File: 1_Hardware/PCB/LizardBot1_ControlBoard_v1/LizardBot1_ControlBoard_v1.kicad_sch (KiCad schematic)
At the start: 12 parts

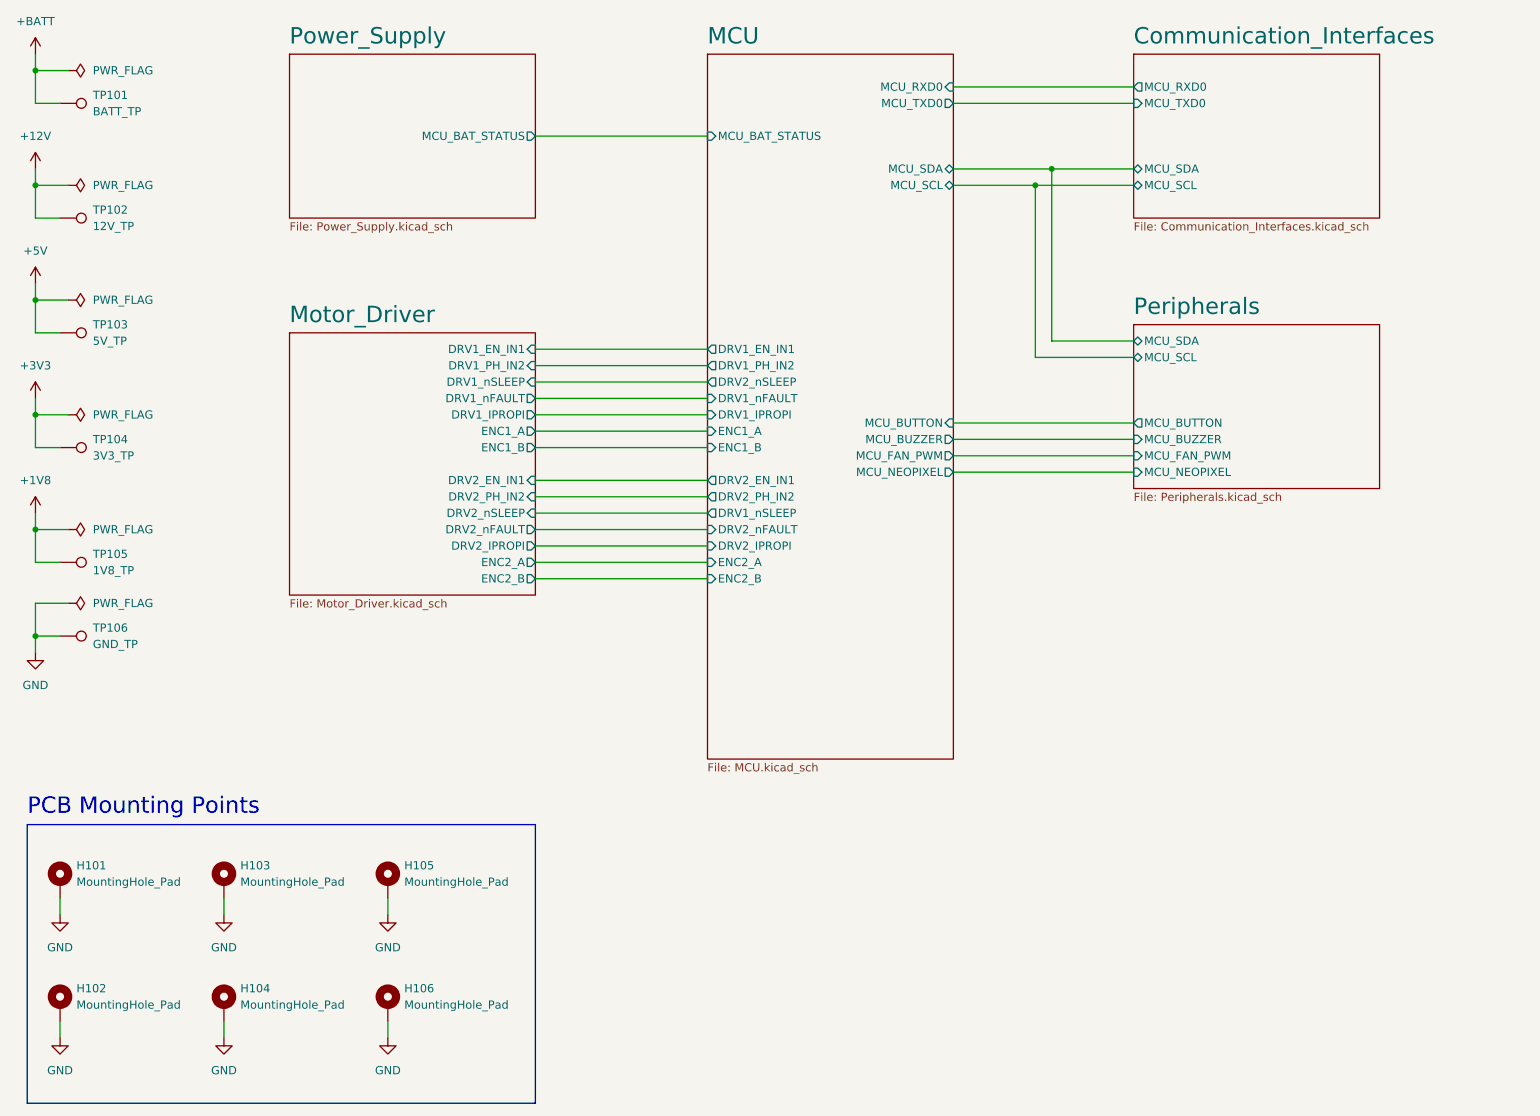
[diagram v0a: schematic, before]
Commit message: Finished PCB routing. Updated ESP32 GPIO layout.
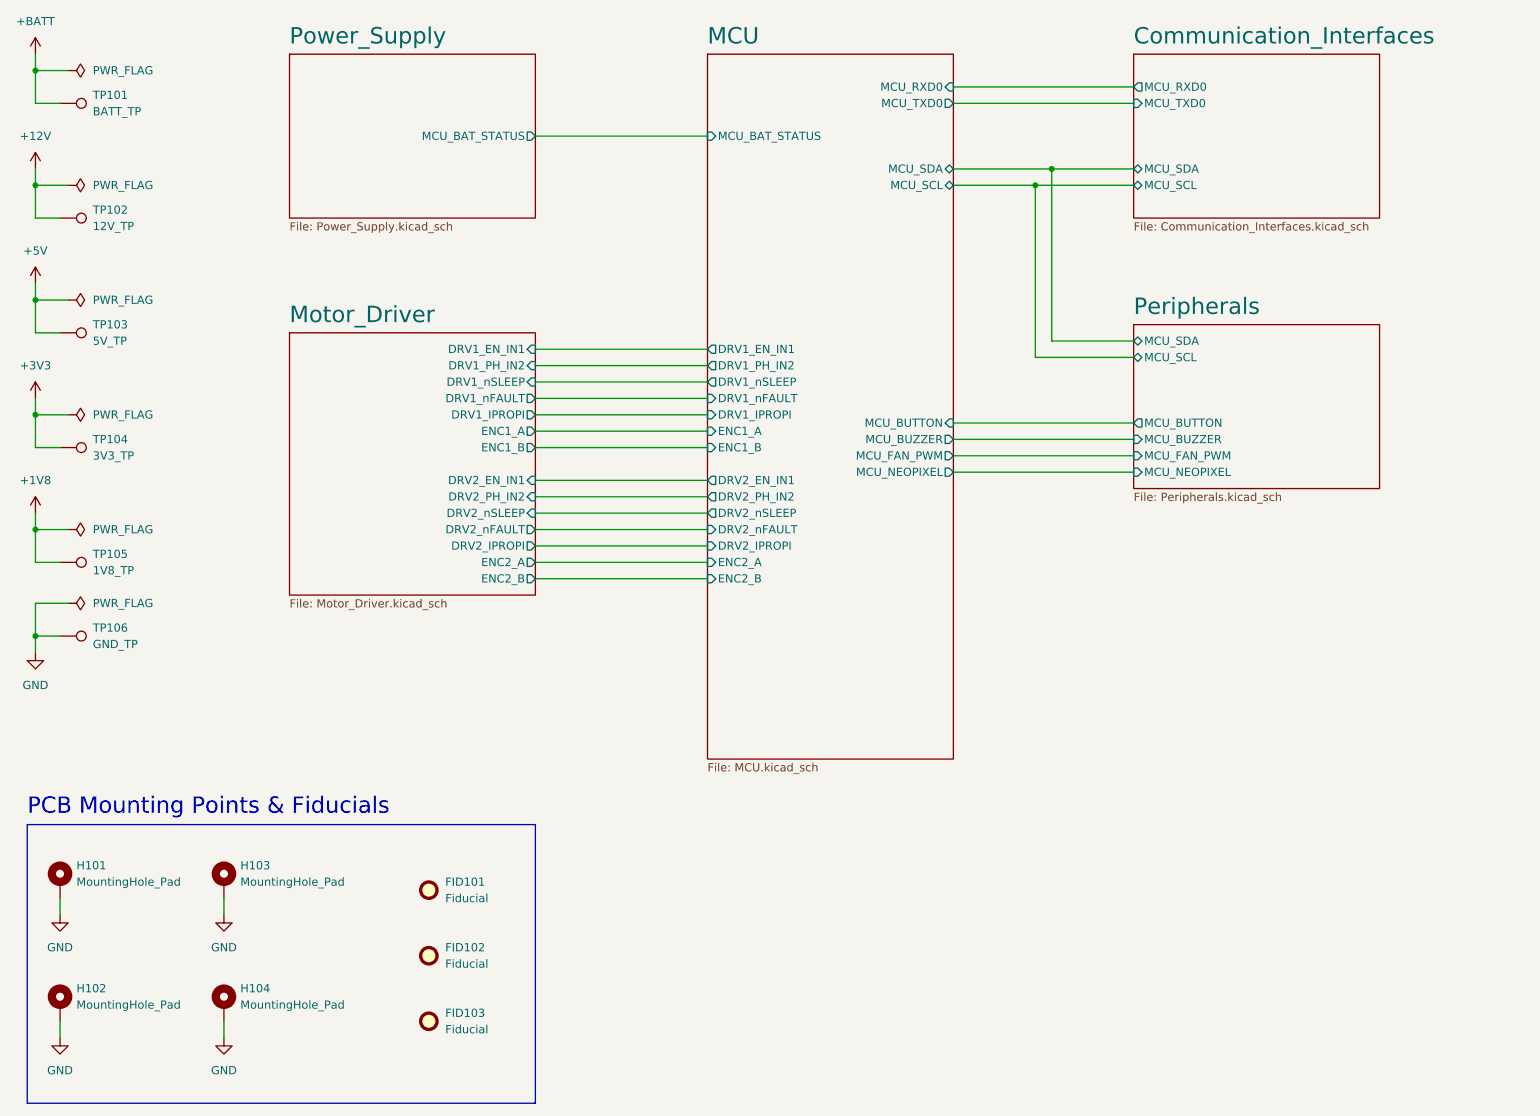
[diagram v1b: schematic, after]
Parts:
- removed H105, H106: MountingHole_Pad, MountingHole:MountingHole_3.2mm_M3_Pad_Via, symbol Mechanical:MountingHole_Pad
- added FID101, FID102, FID103: Fiducial, Fiducial:Fiducial_1mm_Mask2mm, symbol Mechanical:Fiducial
- TP101, TP102, TP103, TP104, TP105, TP106: now left out of the parts list
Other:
- note added: "PCB Mounting Points & Fiducials"
- note removed: "PCB Mounting Points"
